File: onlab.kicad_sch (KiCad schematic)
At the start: 82 parts, among them J1 Battery, J10 DC-Motor, J2 HC_SR04, J3 HC_SR04, J4 HC_SR04, J5 DC-Motor, J6 DC-Motor, J7 DC-Motor, J8 DC-Motor, J9 DC-Motor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

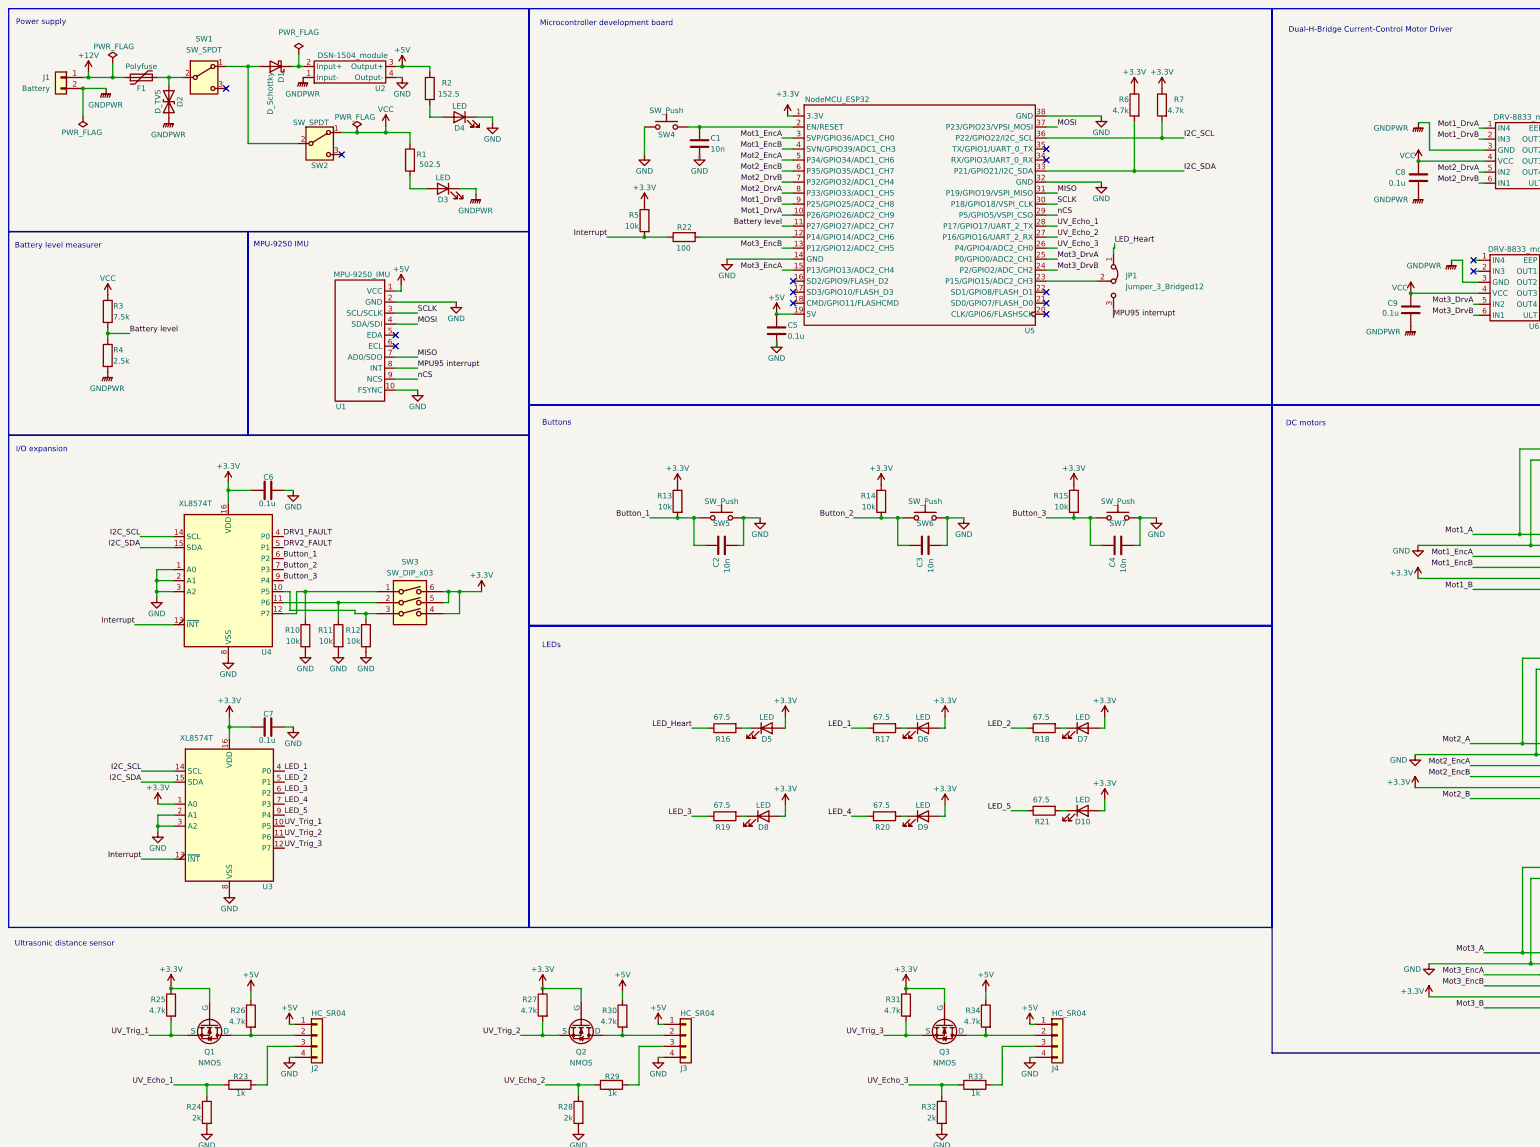
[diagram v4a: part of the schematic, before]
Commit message: Correction of schematic and layout
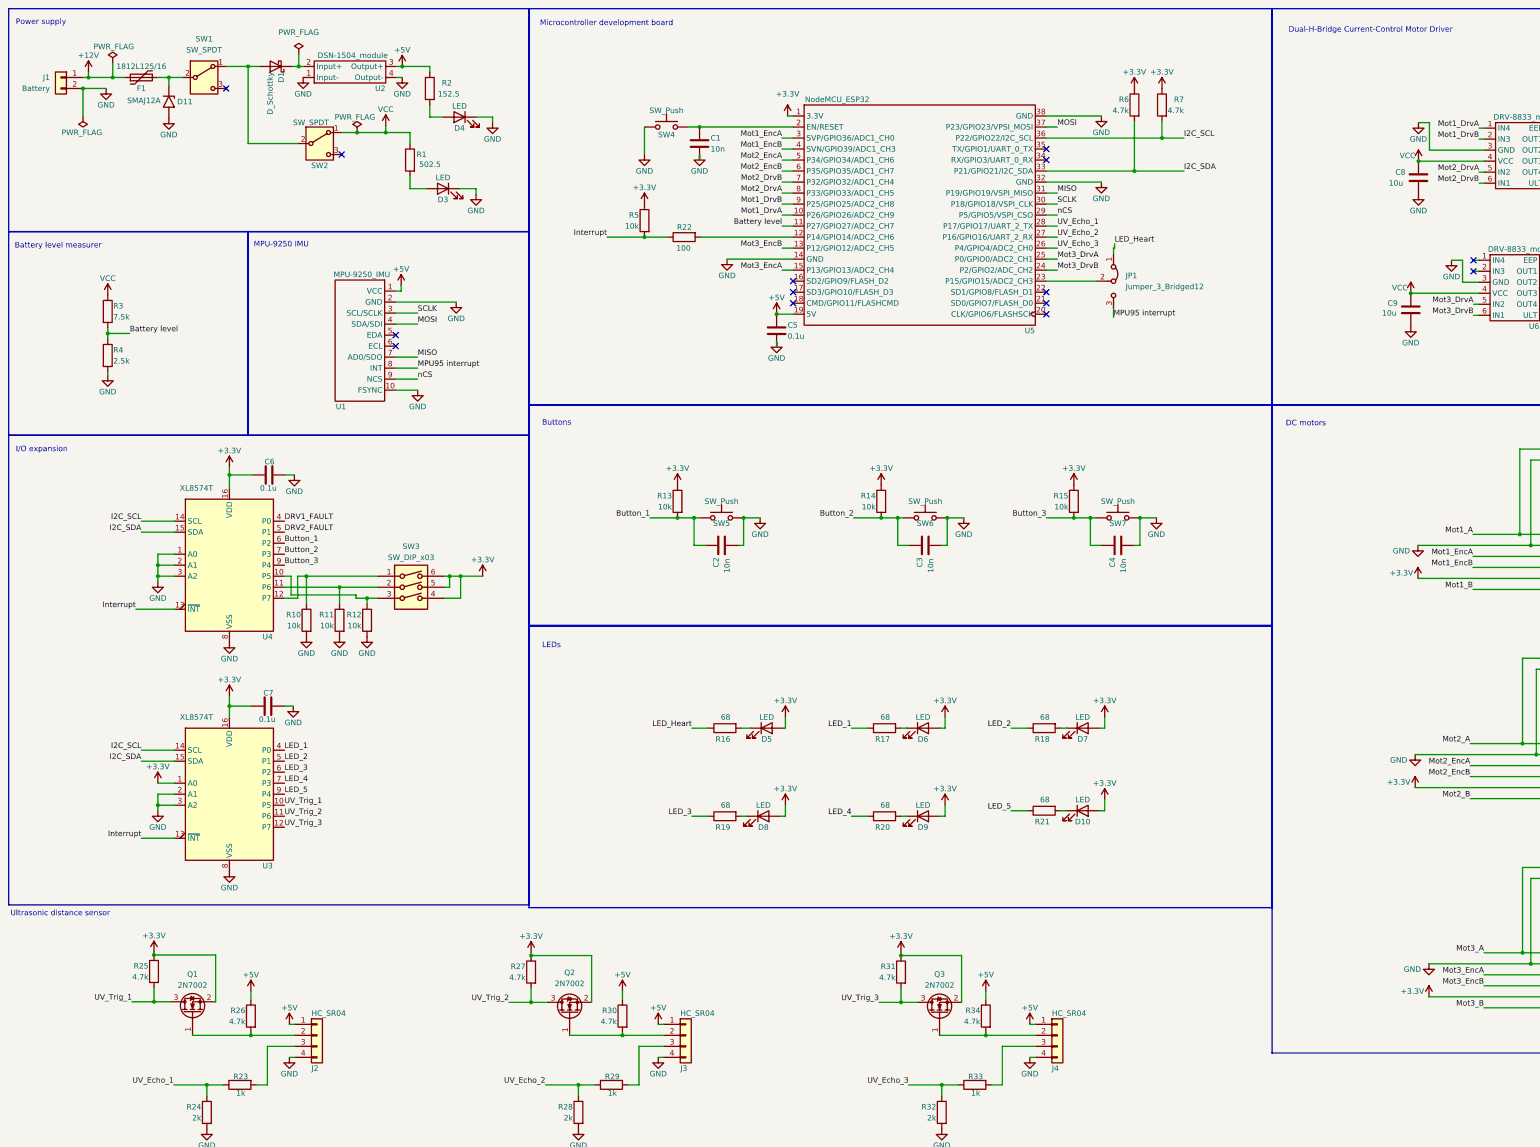
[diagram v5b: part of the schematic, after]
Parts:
- removed D2: D_TVS, Diode_SMD:D_SMA_Handsoldering, symbol Device:D_TVS
- removed Q1, Q2, Q3: NMOS, Package_TO_SOT_SMD:SOT-23_Handsoldering, symbol Simulation_SPICE:NMOS
- added D11: SMAJ12A, Diode_SMD:D_SMA, symbol Diode:SMAJ12A
- added Q1, Q2, Q3: 2N7002, Package_TO_SOT_SMD:SOT-23, symbol Transistor_FET:2N7002
- C8, C9: value 0.1u -> 10u
- F1: value Polyfuse -> 1812L125/16; footprint Fuse:Fuse_0805_2012Metric_Pad1.15x1.40mm_HandSolder -> Onlab:polyfuse
- R16, R17, R18, R19, R20, R21: value 67.5 -> 68
- SW3: footprint Button_Switch_SMD:SW_DIP_SPSTx03_Slide_6.7x9.18mm_W8.61mm_P2.54mm_LowProfile -> Button_Switch_THT:SW_DIP_SPSTx03_Slide_9.78x9.8mm_W7.62mm_P2.54mm
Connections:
- net GNDPWR is gone; now on net GND: C8.2, C9.2, D3.1 (K), J1.2 (Pin_2), R4.2, U2.1 (Input-), U6.3 (GND), U7.3 (GND)
- net +3.3V: now also Q1.2 (S), Q2.2 (S), Q3.2 (S)
- net GND: now also D11.2 (A2)
- net UV_Trig_1: now also Q1.3 (D)
- net UV_Trig_2: now also Q2.3 (D)
- net UV_Trig_3: now also Q3.3 (D)
- net at F1.2, SW1.2 (B): now also D11.1 (A1)
- net at J3.2 (Pin_2), R30.2: now also Q2.1 (G)
- net at J4.2 (Pin_2), R34.2: now also Q3.1 (G)
- net at J2.2 (Pin_2), R26.2: now also Q1.1 (G)
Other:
- moved on the sheet: C6, C7, R10, R11, R12, R25, R27, R31, SW3, U3, U4

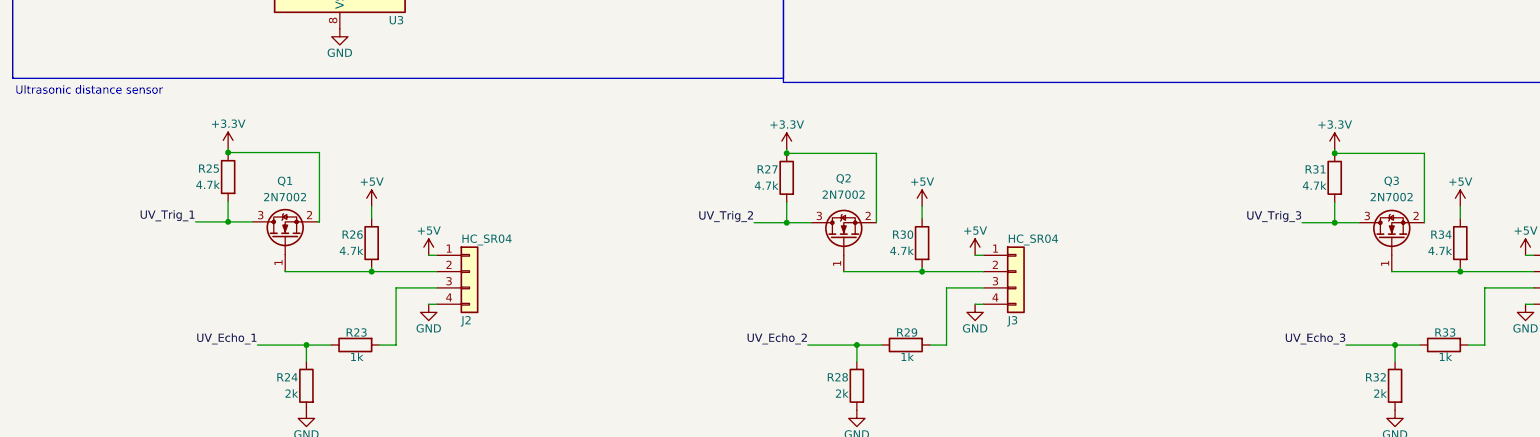
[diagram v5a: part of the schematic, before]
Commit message: Correction of Q1, Q2, Q3 and update of libraries
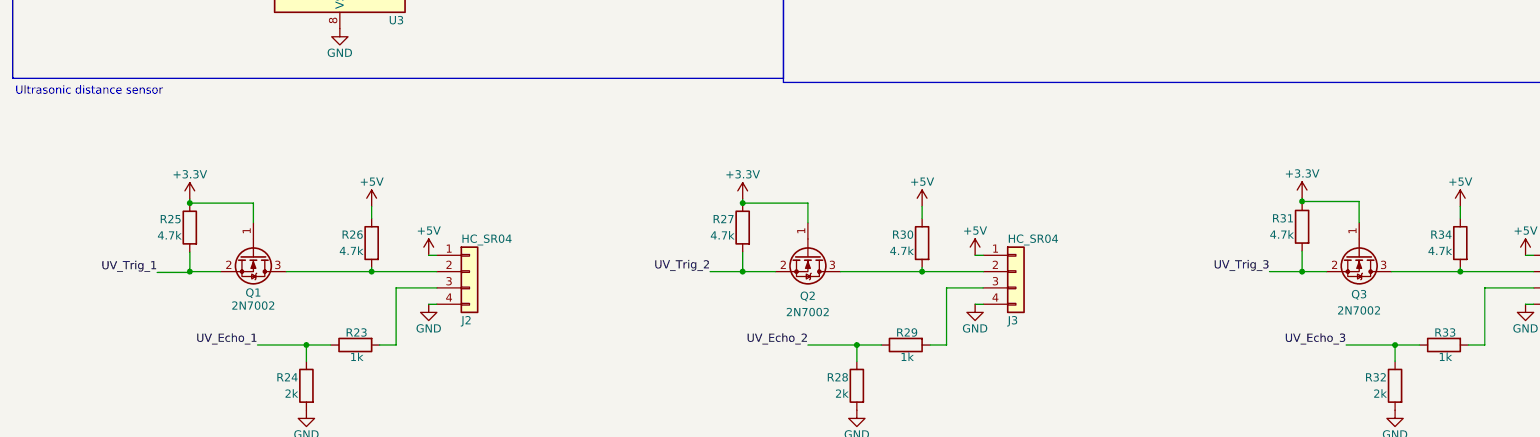
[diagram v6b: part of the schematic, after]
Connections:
- net +3.3V: now also Q1.1 (G), Q2.1 (G), Q3.1 (G); no longer Q1.2 (S), Q2.2 (S), Q3.2 (S)
- net UV_Trig_1: now also Q1.2 (S); no longer Q1.3 (D)
- net UV_Trig_2: now also Q2.2 (S); no longer Q2.3 (D)
- net UV_Trig_3: now also Q3.2 (S); no longer Q3.3 (D)
- net at J4.2 (Pin_2), R34.2: now also Q3.3 (D); no longer Q3.1 (G)
- net at J3.2 (Pin_2), R30.2: now also Q2.3 (D); no longer Q2.1 (G)
- net at J2.2 (Pin_2), R26.2: now also Q1.3 (D); no longer Q1.1 (G)
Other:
- moved on the sheet: R25, R27, R31

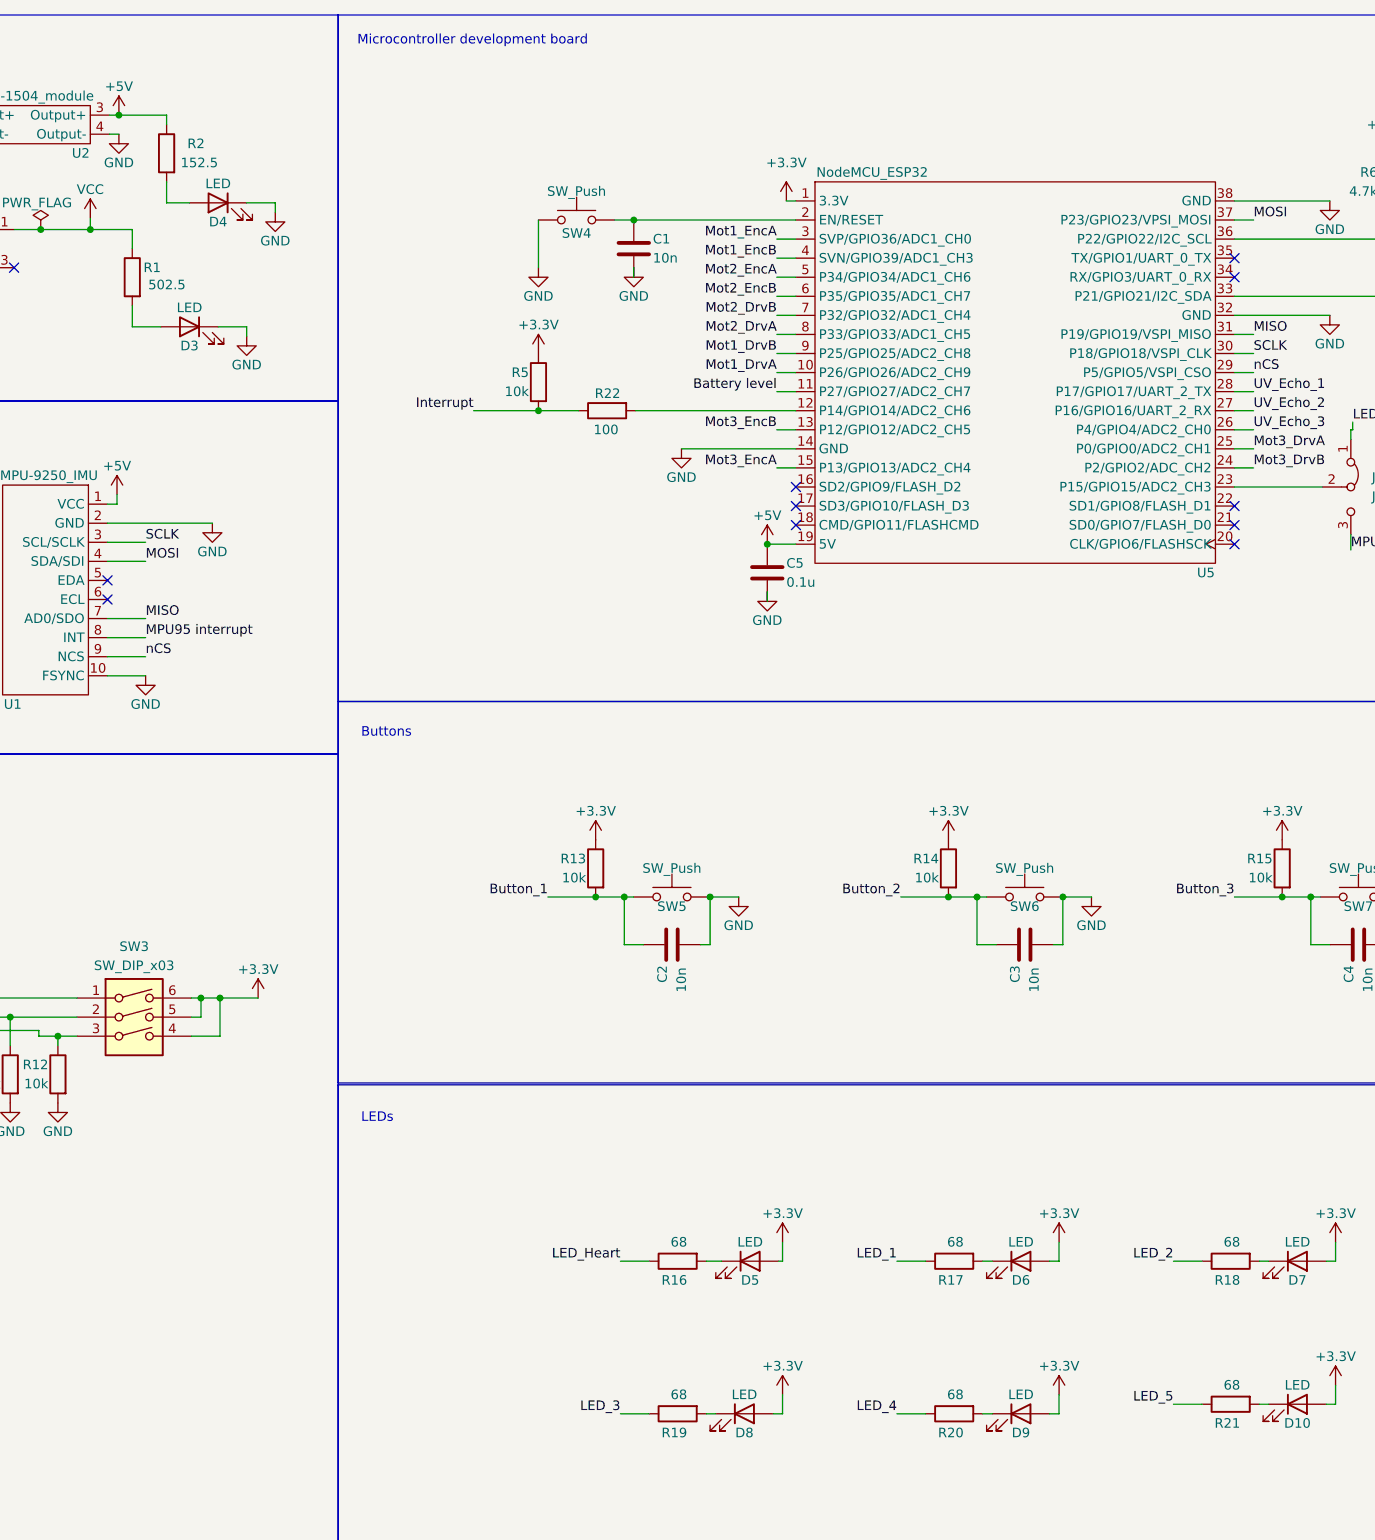
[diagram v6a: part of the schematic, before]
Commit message: resistor value update
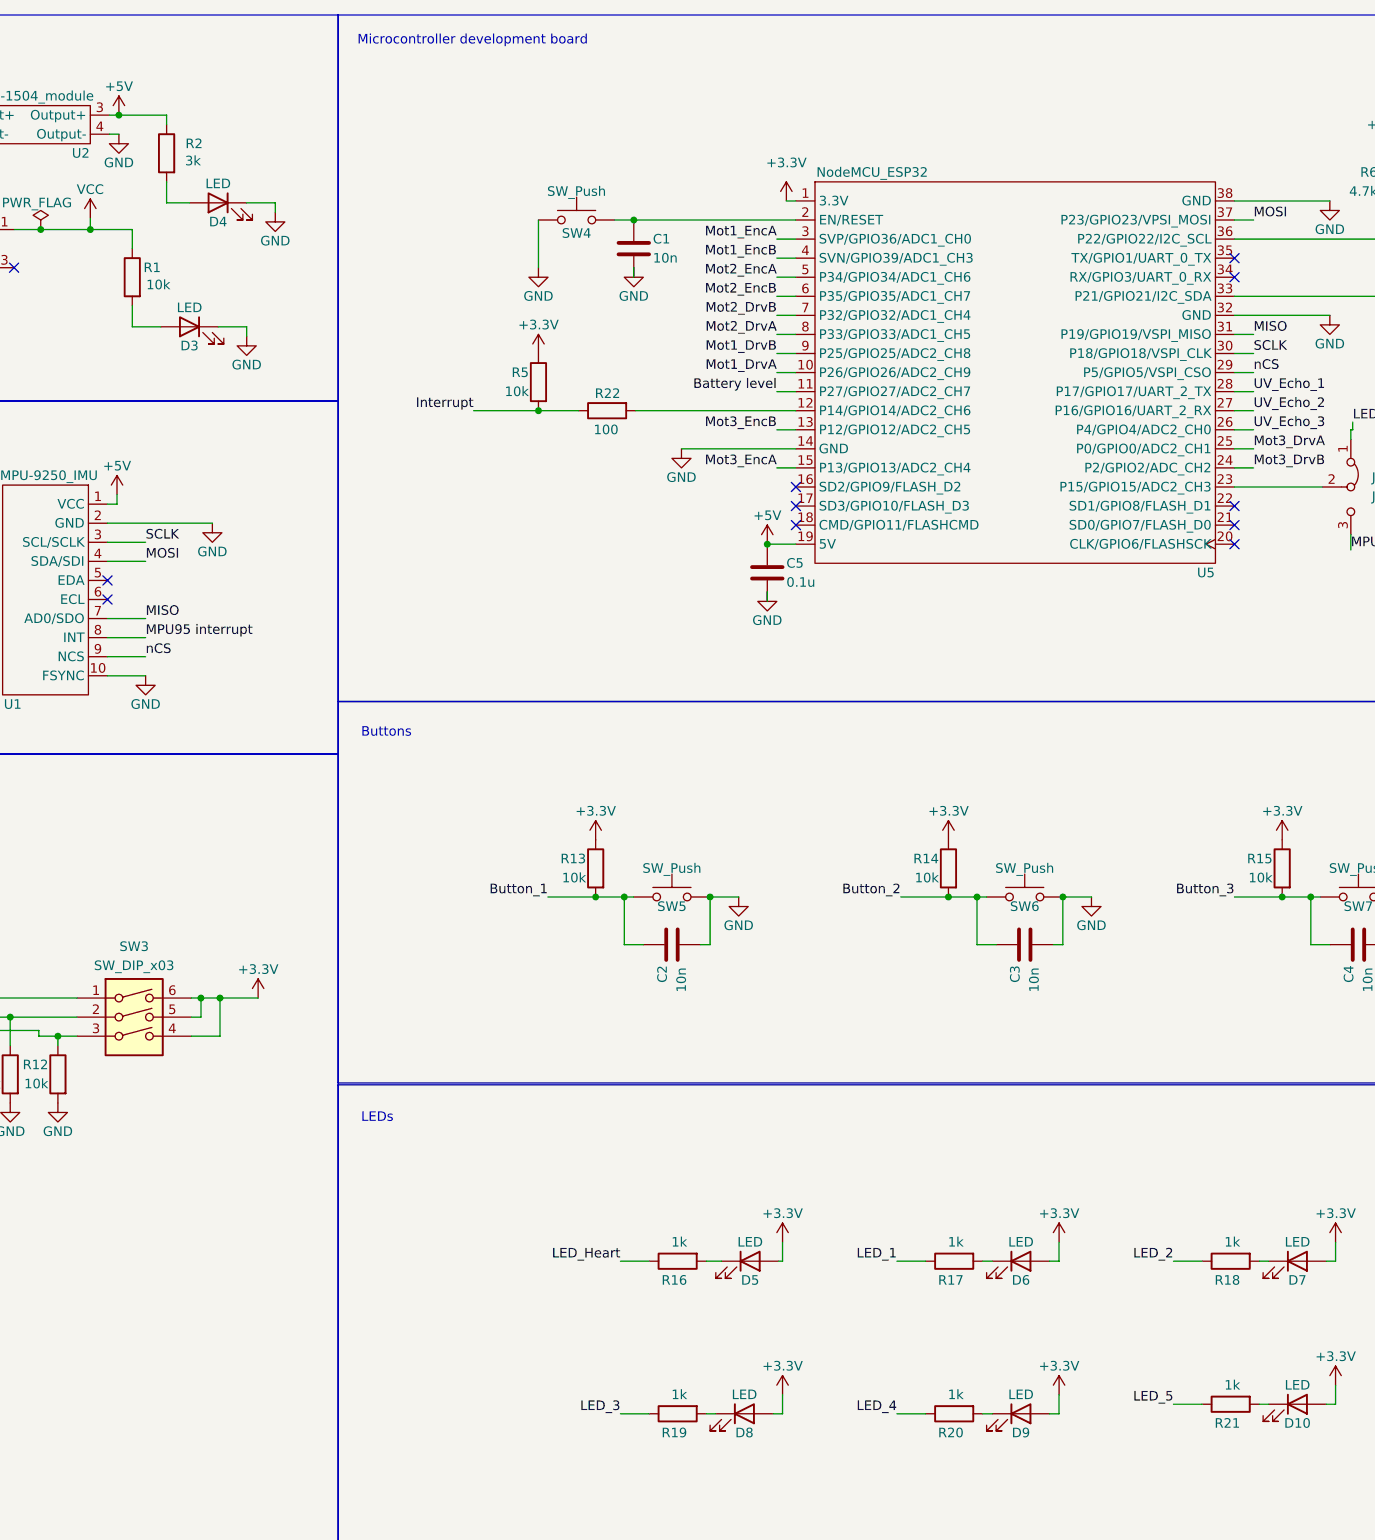
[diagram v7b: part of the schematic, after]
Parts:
- R1: value 502.5 -> 10k
- R16, R17, R18, R19, R20, R21: value 68 -> 1k
- R2: value 152.5 -> 3k
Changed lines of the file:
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@@
 			)
 		)
-		(property "Value" "68"
+		(property "Value" "1k"
 			(at 252.222 194.564 90)
 			(effects
@@
 			)
 		)
-		(property "Value" "68"
+		(property "Value" "1k"
 			(at 215.392 195.834 90)
 			(effects
@@
 			)
 		)
-		(property "Value" "68"
+		(property "Value" "1k"
 			(at 215.392 175.514 90)
 			(effects
@@
 			)
 		)
-		(property "Value" "68"
+		(property "Value" "1k"
 			(at 178.562 195.834 90)
 			(effects
@@
 		(dnp no)
 		(property "Reference" "R2"
-			(at 114.3 29.21 0)
+			(at 114.046 29.21 0)
 			(effects
 				(font
@@
 			)
 		)
-		(property "Value" "152.5"
-			(at 116.078 31.75 0)
+		(property "Value" "3k"
+			(at 113.792 31.496 0)
 			(effects
 				(font
@@
 			)
 		)
-		(property "Value" "502.5"
-			(at 111.76 48.006 0)
+		(property "Value" "10k"
+			(at 109.728 48.006 0)
 			(effects
 				(font
@@
 			)
 		)
-		(property "Value" "68"
+		(property "Value" "1k"
 			(at 252.222 175.514 90)
 			(effects
@@
 			)
 		)
-		(property "Value" "68"
+		(property "Value" "1k"
 			(at 178.562 175.514 90)
 			(effects
